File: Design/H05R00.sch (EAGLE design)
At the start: 55 parts, among them Q1 ECH8693R-TL-W, U1 STM32G0B1CEU6N, U2 MAX17330X22+, U3 TPS631000DRLR, U4 LD39200PU33R, X1 XTALL_CSTCE8M00G52

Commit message: -The final design filles (for this version)
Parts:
- removed BAT: B2B-PH-K-S(LF)(SN), HEXABITZ_CONNECTION_PARTS:B2B-PH-K-S(LF)(SN)
- removed PWR: USB_B_MICRO, HEXABITZ_CONNECTION_PARTS:629105136821
- added BAT_J: B2B-PH-K-S(LF)(SN), HEXABITZ_CONNECTION_PARTS:B2B-PH-K-S(LF)(SN)
- added C16: 22pF, HEXABITZ_RCLS:C-0603
- added D3: GREEN, Hexabitz:VLMS1300-GS08
- added EXT_TH_J: 3-644456-2, HEXABITZ_USER_INTERFACE_PARTS:3-644456-2
- added R24: 270R, HEXABITZ_RCLS:R-0603
- added USB_C: UJC-HP-G-SMT-TR, HEXABITZ_CONNECTION_PARTS:UJC-HP-G-SMT-TR
- C10: VOLTAGE_RATING 10V -> 6.3V
- C8: value 22uF/10V -> 22uF; VOLTAGE (none) -> 10V
- R13, R14: MPN (none) -> NCP18XH103F03RB
- R22: value 10K -> 100K
- R23: value 100 -> DNP; RESISTANCE (none) -> 100R
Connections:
- net N$23 renamed BAT_ALRT
- net N$24 renamed BAT_SDA
- net N$25 renamed BAT_SCL
- removed net ALRT: R16.1, R22.1
- removed net CSN: C18.1, Q1.SOURCE1, R4.2, U2.CSN
- removed net N$22: C13.1, R12.2
- removed net SCL: R15.1, R21.1
- removed net SDA: R11.1, R17.1
- removed net USART4_RX: U1.PA1
- removed net USART4_TX: U1.PA0
- new net CSP: C18.1, Q1.SOURCE1, R4.2, U2.CSP
- new net MCU_INT: R16.1, R22.1, U1.PB0
- new net MCU_SCL: R15.1, R21.1, U1.PA7
- new net MCU_SDA: R11.1, R17.1, U1.PA6
- new net N$3: D3.A, R24.2
- new net STATUS_LED: R24.1, U1.PB4
- net +3.8V: now also C16.1
- net GND: now also D3.C
- net N$18: now also EXT_TH_J.2
- net N$21: now also C13.1
- net N$27: now also C16.2
- net USART1_RX: now also U$1.SD5
- net USART1_TX: now also U$1.SU5
- net USART2_RX: now also U$1.SD2
- net USART2_TX: now also U$1.SU2
- net USART3_RX: now also U$1.SD4
- net USART3_TX: now also U$1.SU4
- net USART5_RX: now also U$1.SD1
- net USART5_TX: now also U$1.SU1
- net USART6_RX: now also U$1.SD3
- net USART6_TX: now also U$1.SU3
- net VBAT: now also BAT_J.1, R12.2, U2.CSN; no longer BAT.1, U2.CSP
- net VBUS: now also USB_C.VBUS; no longer PWR.1
- net VSSA: now also BAT_J.2, EXT_TH_J.1, USB_C.GND, USB_C.SHIELD; no longer BAT.2, PWR.4, PWR.5, PWR.SHIELD
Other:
- note added: "1s Lipo charger w/ USB-C"
- note added: "BAT_I2C"
- note added: "Battery input"
- note added: "Buck-Boost Converter"
- note added: "Charge & Discharge N-FET"
- note added: "Charger , fuel gauge and protector"
- note added: "LDO Regulator"
- note added: "MAX OUTPUT CURRENT = 2 A"
- note added: "Power input"
- note added: "VBAT RANGE = (2.16 - 4.9 ) Volt"
- note added: "VBUS RANGE = (1.65 - 5.5 ) Volt"
- note removed: "1s Lipo charger w/ DC input or USB"
- moved on the sheet: C1, C10, C11, C12, C13, C14, C15, C17, C18, C8, C9, D1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

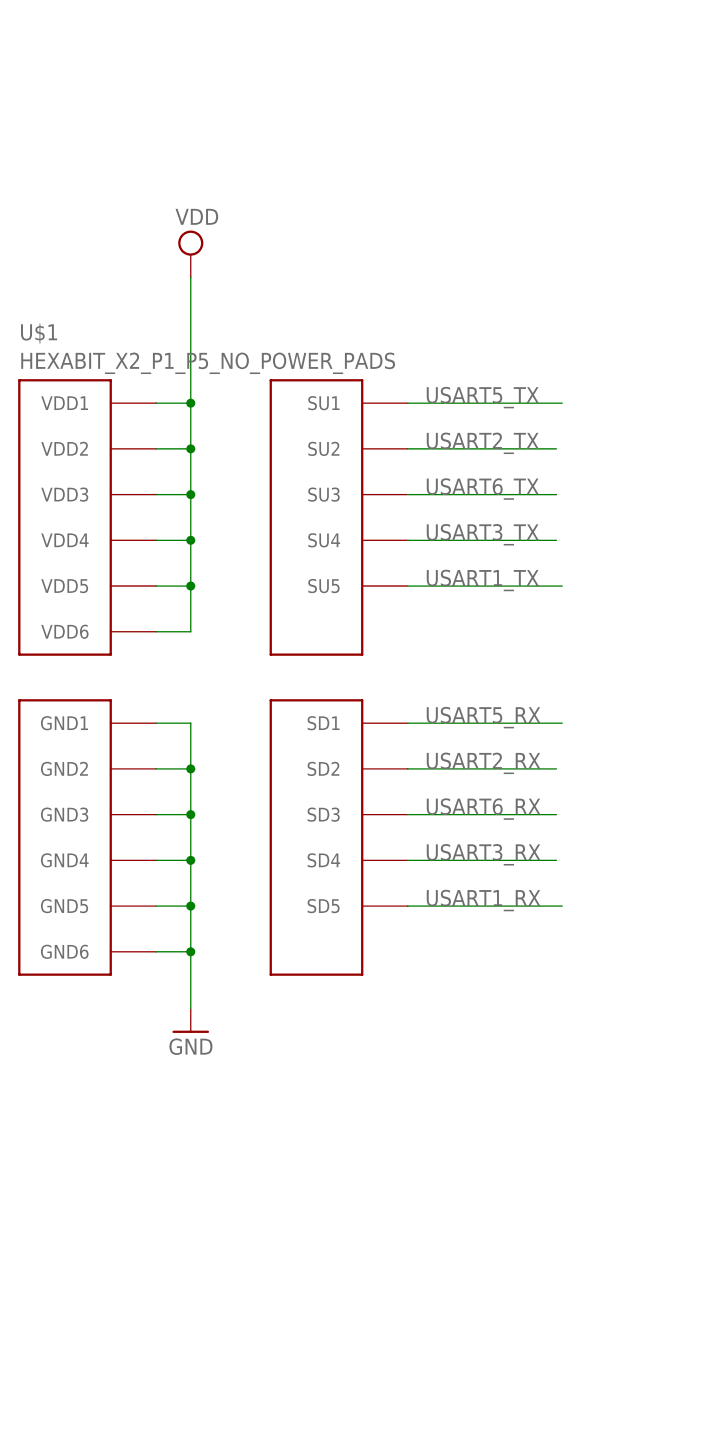
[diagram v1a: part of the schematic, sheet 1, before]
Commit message: - Add power pads for the power hexagon and improve the silkscreen layer look
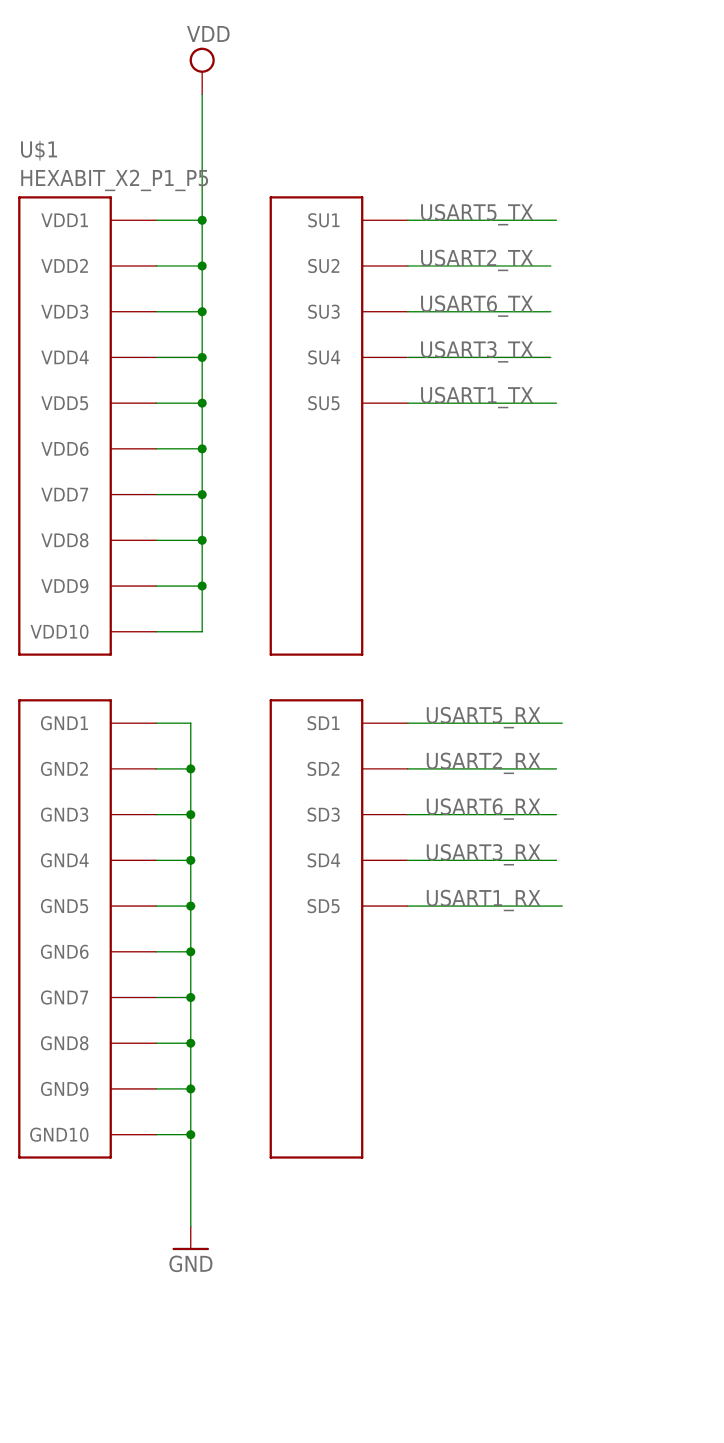
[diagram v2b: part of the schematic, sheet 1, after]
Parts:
- U$1: value HEXABIT_X2_P1_P5_NO_POWER_PADS -> HEXABIT_X2_P1_P5; device hexabitz_connectors:HEXABIT_X2_P1_P5_NO_POWER_PADS -> hexabitz_connectors:HEXABIT_X2_P1_P5
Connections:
- net GND: now also U$1.GND10, U$1.GND7, U$1.GND8, U$1.GND9
- net VDD: now also U$1.VDD10, U$1.VDD7, U$1.VDD8, U$1.VDD9
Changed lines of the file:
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@@
 <part name="GND3" library="supply1" deviceset="GND" device=""/>
 <part name="GND12" library="supply1" deviceset="GND" device=""/>
-<part name="U$1" library="hexabitz_connectors" library_urn="urn:adsk.eagle:library:20064578" deviceset="HEXABIT_X2_P1_P5_NO_POWER_PADS" device="" package3d_urn="urn:adsk.eagle:package:41856122/1"/>
+<part name="U$1" library="hexabitz_connectors" library_urn="urn:adsk.eagle:library:20064578" deviceset="HEXABIT_X2_P1_P5" device="" package3d_urn="urn:adsk.eagle:package:28065030/1"/>
 <part name="SUPPLY1" library="supply2" deviceset="VBAT" device=""/>
 <part name="SUPPLY26" library="supply2" deviceset="VBAT" device=""/>
@@
 <attribute name="VALUE" x="142.875" y="103.505" size="1.778" layer="96" rot="MR0"/>
 </instance>
-<instance part="SUPPLY33" gate="G$1" x="36.83" y="184.15" smashed="yes">
-<attribute name="VALUE" x="40.005" y="189.23" size="1.778" layer="96" rot="R180"/>
-</instance>
-<instance part="GND7" gate="1" x="36.83" y="97.79" smashed="yes" rot="MR0">
-<attribute name="VALUE" x="39.37" y="95.25" size="1.778" layer="96" rot="MR0"/>
+<instance part="SUPPLY33" gate="G$1" x="38.1" y="204.47" smashed="yes">
+<attribute name="VALUE" x="41.275" y="209.55" size="1.778" layer="96" rot="R180"/>
+</instance>
+<instance part="GND7" gate="1" x="36.83" y="73.66" smashed="yes" rot="MR0">
+<attribute name="VALUE" x="39.37" y="71.12" size="1.778" layer="96" rot="MR0"/>
 </instance>
 <instance part="U$1" gate="G$1" x="38.1" y="137.16" smashed="yes">
-<attribute name="NAME" x="17.78" y="174.625" size="1.778" layer="95"/>
-<attribute name="VALUE" x="17.78" y="171.45" size="1.778" layer="96"/>
+<attribute name="NAME" x="17.78" y="194.945" size="1.778" layer="95"/>
+<attribute name="VALUE" x="17.78" y="191.77" size="1.778" layer="96"/>
 </instance>
 </instances>
@@
 <wire x1="36.83" y1="116.84" x2="36.83" y2="111.76" width="0.1524" layer="91"/>
 <wire x1="36.83" y1="111.76" x2="36.83" y2="106.68" width="0.1524" layer="91"/>
-<wire x1="36.83" y1="106.68" x2="36.83" y2="100.33" width="0.1524" layer="91"/>
+<wire x1="36.83" y1="106.68" x2="36.83" y2="101.6" width="0.1524" layer="91"/>
+<wire x1="36.83" y1="101.6" x2="36.83" y2="96.52" width="0.1524" layer="91"/>
+<wire x1="36.83" y1="96.52" x2="36.83" y2="91.44" width="0.1524" layer="91"/>
+<wire x1="36.83" y1="91.44" x2="36.83" y2="86.36" width="0.1524" layer="91"/>
+<wire x1="36.83" y1="86.36" x2="36.83" y2="76.2" width="0.1524" layer="91"/>
 <wire x1="33.02" y1="106.68" x2="36.83" y2="106.68" width="0.1524" layer="91"/>
 <wire x1="33.02" y1="111.76" x2="36.83" y2="111.76" width="0.1524" layer="91"/>
@@
 <pinref part="U$1" gate="G$1" pin="GND5"/>
 <pinref part="U$1" gate="G$1" pin="GND6"/>
+<pinref part="U$1" gate="G$1" pin="GND7"/>
+<wire x1="33.02" y1="101.6" x2="36.83" y2="101.6" width="0.1524" layer="91"/>
+<junction x="36.83" y="101.6"/>
+<pinref part="U$1" gate="G$1" pin="GND8"/>
+<wire x1="33.02" y1="96.52" x2="36.83" y2="96.52" width="0.1524" layer="91"/>
+<junction x="36.83" y="96.52"/>
+<pinref part="U$1" gate="G$1" pin="GND9"/>
+<wire x1="33.02" y1="91.44" x2="36.83" y2="91.44" width="0.1524" layer="91"/>
+<junction x="36.83" y="91.44"/>
+<pinref part="U$1" gate="G$1" pin="GND10"/>
+<wire x1="33.02" y1="86.36" x2="36.83" y2="86.36" width="0.1524" layer="91"/>
+<junction x="36.83" y="86.36"/>
 </segment>
 </net>
@@
 </segment>
 <segment>
-<wire x1="77.47" y1="152.4" x2="60.96" y2="152.4" width="0.1524" layer="91"/>
+<wire x1="76.835" y1="172.72" x2="60.96" y2="172.72" width="0.1524" layer="91"/>
 <pinref part="U$1" gate="G$1" pin="SU4"/>
-<label x="62.865" y="152.4" size="1.778" layer="95"/>
+<label x="62.23" y="172.72" size="1.778" layer="95"/>
 </segment>
 </net>
@@
 </segment>
 <segment>
-<wire x1="60.96" y1="162.56" x2="77.47" y2="162.56" width="0.1524" layer="91"/>
+<wire x1="60.96" y1="182.88" x2="76.835" y2="182.88" width="0.1524" layer="91"/>
 <pinref part="U$1" gate="G$1" pin="SU2"/>
-<label x="62.865" y="162.56" size="1.778" layer="95"/>
+<label x="62.23" y="182.88" size="1.778" layer="95"/>
 </segment>
 </net>
@@
 </segment>
 <segment>
-<wire x1="60.96" y1="167.64" x2="78.105" y2="167.64" width="0.1524" layer="91"/>
+<wire x1="60.96" y1="187.96" x2="77.47" y2="187.96" width="0.1524" layer="91"/>
 <pinref part="U$1" gate="G$1" pin="SU1"/>
-<label x="62.865" y="167.64" size="1.778" layer="95"/>
+<label x="62.23" y="187.96" size="1.778" layer="95"/>
 </segment>
 </net>
@@
 </segment>
 <segment>
-<wire x1="60.96" y1="147.32" x2="78.105" y2="147.32" width="0.1524" layer="91"/>
+<wire x1="60.96" y1="167.64" x2="77.47" y2="167.64" width="0.1524" layer="91"/>
 <pinref part="U$1" gate="G$1" pin="SU5"/>
-<label x="62.865" y="147.32" size="1.778" layer="95"/>
+<label x="62.23" y="167.64" size="1.778" layer="95"/>
 </segment>
 </net>
@@
 </segment>
 <segment>
-<wire x1="60.96" y1="157.48" x2="77.47" y2="157.48" width="0.1524" layer="91"/>
+<wire x1="60.96" y1="177.8" x2="76.835" y2="177.8" width="0.1524" layer="91"/>
 <pinref part="U$1" gate="G$1" pin="SU3"/>
-<label x="62.865" y="157.48" size="1.778" layer="95"/>
+<label x="62.23" y="177.8" size="1.778" layer="95"/>
 </segment>
 </net>
@@
 <net name="VDD" class="0">
 <segment>
-<wire x1="36.83" y1="167.64" x2="36.83" y2="162.56" width="0.1524" layer="91"/>
-<wire x1="36.83" y1="162.56" x2="36.83" y2="157.48" width="0.1524" layer="91"/>
-<wire x1="36.83" y1="157.48" x2="36.83" y2="152.4" width="0.1524" layer="91"/>
-<wire x1="36.83" y1="152.4" x2="36.83" y2="147.32" width="0.1524" layer="91"/>
-<wire x1="36.83" y1="147.32" x2="36.83" y2="142.24" width="0.1524" layer="91"/>
-<wire x1="36.83" y1="142.24" x2="33.02" y2="142.24" width="0.1524" layer="91"/>
-<wire x1="33.02" y1="147.32" x2="36.83" y2="147.32" width="0.1524" layer="91"/>
-<wire x1="33.02" y1="152.4" x2="36.83" y2="152.4" width="0.1524" layer="91"/>
-<wire x1="33.02" y1="157.48" x2="36.83" y2="157.48" width="0.1524" layer="91"/>
-<wire x1="33.02" y1="162.56" x2="36.83" y2="162.56" width="0.1524" layer="91"/>
-<wire x1="33.02" y1="167.64" x2="36.83" y2="167.64" width="0.1524" layer="91"/>
-<junction x="36.83" y="162.56"/>
-<junction x="36.83" y="157.48"/>
-<junction x="36.83" y="152.4"/>
-<junction x="36.83" y="147.32"/>
+<wire x1="38.1" y1="187.96" x2="38.1" y2="182.88" width="0.1524" layer="91"/>
+<wire x1="38.1" y1="182.88" x2="38.1" y2="177.8" width="0.1524" layer="91"/>
+<wire x1="38.1" y1="177.8" x2="38.1" y2="172.72" width="0.1524" layer="91"/>
+<wire x1="38.1" y1="172.72" x2="38.1" y2="167.64" width="0.1524" layer="91"/>
+<wire x1="38.1" y1="167.64" x2="38.1" y2="162.56" width="0.1524" layer="91"/>
+<wire x1="38.1" y1="162.56" x2="33.02" y2="162.56" width="0.1524" layer="91"/>
+<wire x1="33.02" y1="167.64" x2="38.1" y2="167.64" width="0.1524" layer="91"/>
+<wire x1="33.02" y1="172.72" x2="38.1" y2="172.72" width="0.1524" layer="91"/>
+<wire x1="33.02" y1="177.8" x2="38.1" y2="177.8" width="0.1524" layer="91"/>
+<wire x1="33.02" y1="182.88" x2="38.1" y2="182.88" width="0.1524" layer="91"/>
+<wire x1="33.02" y1="187.96" x2="38.1" y2="187.96" width="0.1524" layer="91"/>
+<junction x="38.1" y="182.88"/>
+<junction x="38.1" y="177.8"/>
+<junction x="38.1" y="172.72"/>
+<junction x="38.1" y="167.64"/>
 <pinref part="U$1" gate="G$1" pin="VDD1"/>
 <pinref part="U$1" gate="G$1" pin="VDD2"/>
@@
 <pinref part="U$1" gate="G$1" pin="VDD6"/>
 <pinref part="SUPPLY33" gate="G$1" pin="VDD"/>
-<wire x1="36.83" y1="181.61" x2="36.83" y2="167.64" width="0.1524" layer="91"/>
-<junction x="36.83" y="167.64"/>
-</segment>
-<segment>
+<wire x1="38.1" y1="201.93" x2="38.1" y2="187.96" width="0.1524" layer="91"/>
+<junction x="38.1" y="187.96"/>
+<pinref part="U$1" gate="G$1" pin="VDD10"/>
+<wire x1="33.02" y1="142.24" x2="38.1" y2="142.24" width="0.1524" layer="91"/>
+<wire x1="38.1" y1="142.24" x2="38.1" y2="147.32" width="0.1524" layer="91"/>
+<junction x="38.1" y="162.56"/>
+<pinref part="U$1" gate="G$1" pin="VDD7"/>
+<wire x1="38.1" y1="147.32" x2="38.1" y2="152.4" width="0.1524" layer="91"/>
+<wire x1="38.1" y1="152.4" x2="38.1" y2="157.48" width="0.1524" layer="91"/>
+<wire x1="38.1" y1="157.48" x2="38.1" y2="162.56" width="0.1524" layer="91"/>
+<wire x1="33.02" y1="157.48" x2="38.1" y2="157.48" width="0.1524" layer="91"/>
+<junction x="38.1" y="157.48"/>
+<pinref part="U$1" gate="G$1" pin="VDD8"/>
+<wire x1="33.02" y1="152.4" x2="38.1" y2="152.4" width="0.1524" layer="91"/>
+<junction x="38.1" y="152.4"/>
+<pinref part="U$1" gate="G$1" pin="VDD9"/>
+<wire x1="38.1" y1="147.32" x2="33.02" y2="147.32" width="0.1524" layer="91"/>
+<junction x="38.1" y="147.32"/>
+</segment>
+<segment>
